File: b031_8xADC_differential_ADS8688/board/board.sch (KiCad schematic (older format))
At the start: 18 parts, among them J1 002_SPI_2x5, J2 007_ADC_2x5, J3 007_ADC_2x5, J4 007_ADC_2x5, J5 007_ADC_2x5, J6 007_ADC_2x5, J7 007_ADC_2x5, J8 007_ADC_2x5, J9 007_ADC_2x5, U1 ADS8688

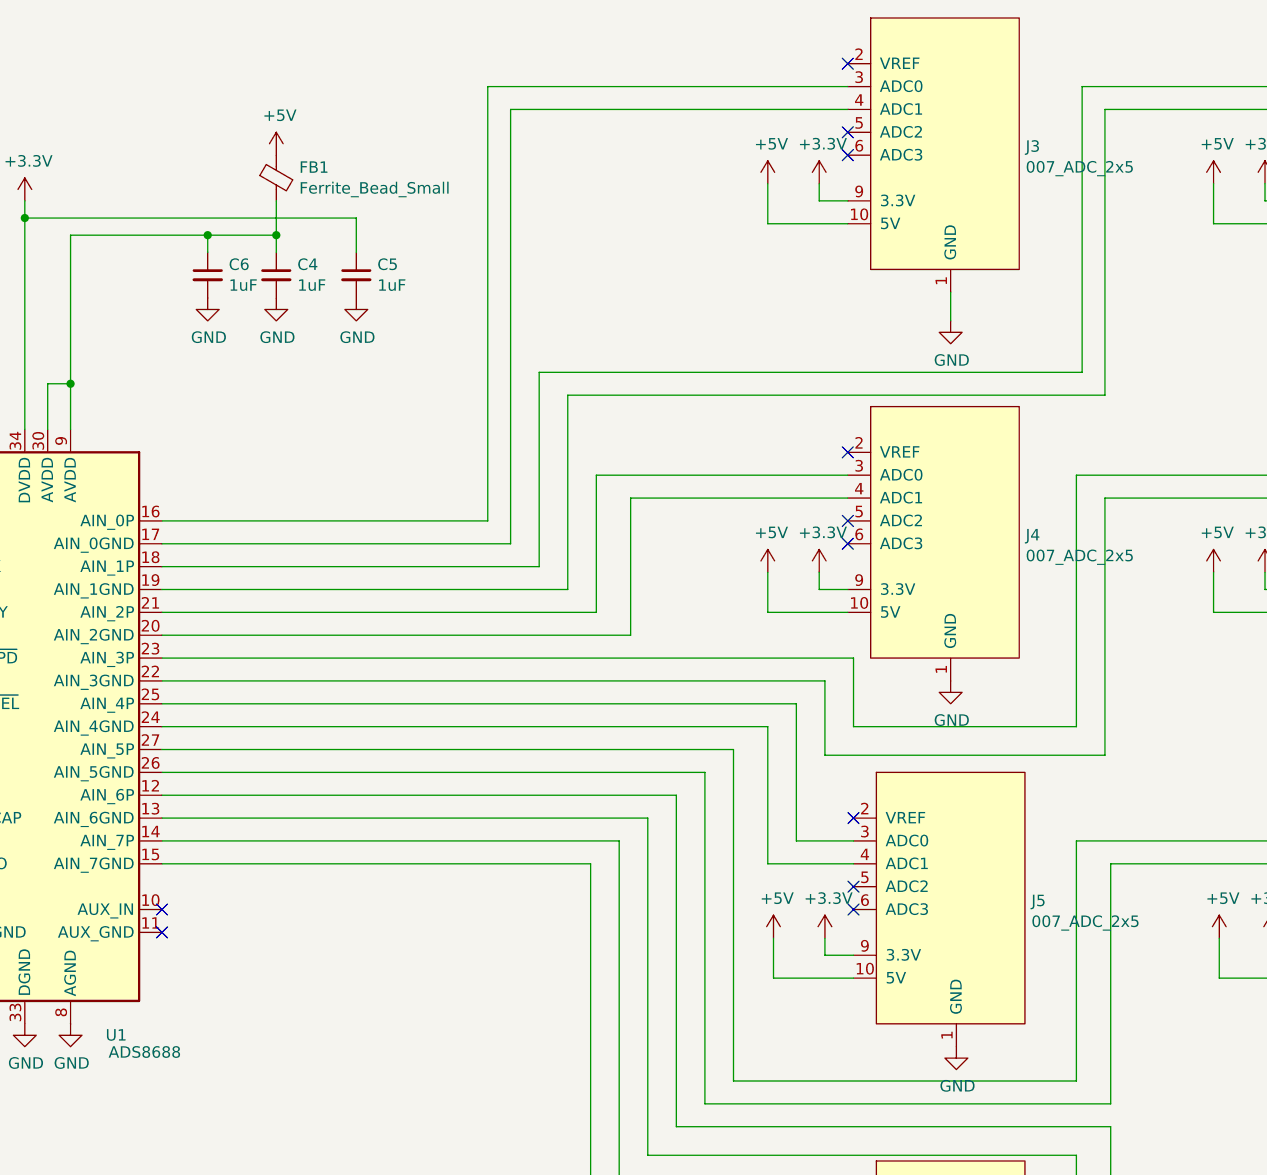
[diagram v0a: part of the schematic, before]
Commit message: added gnd resistors
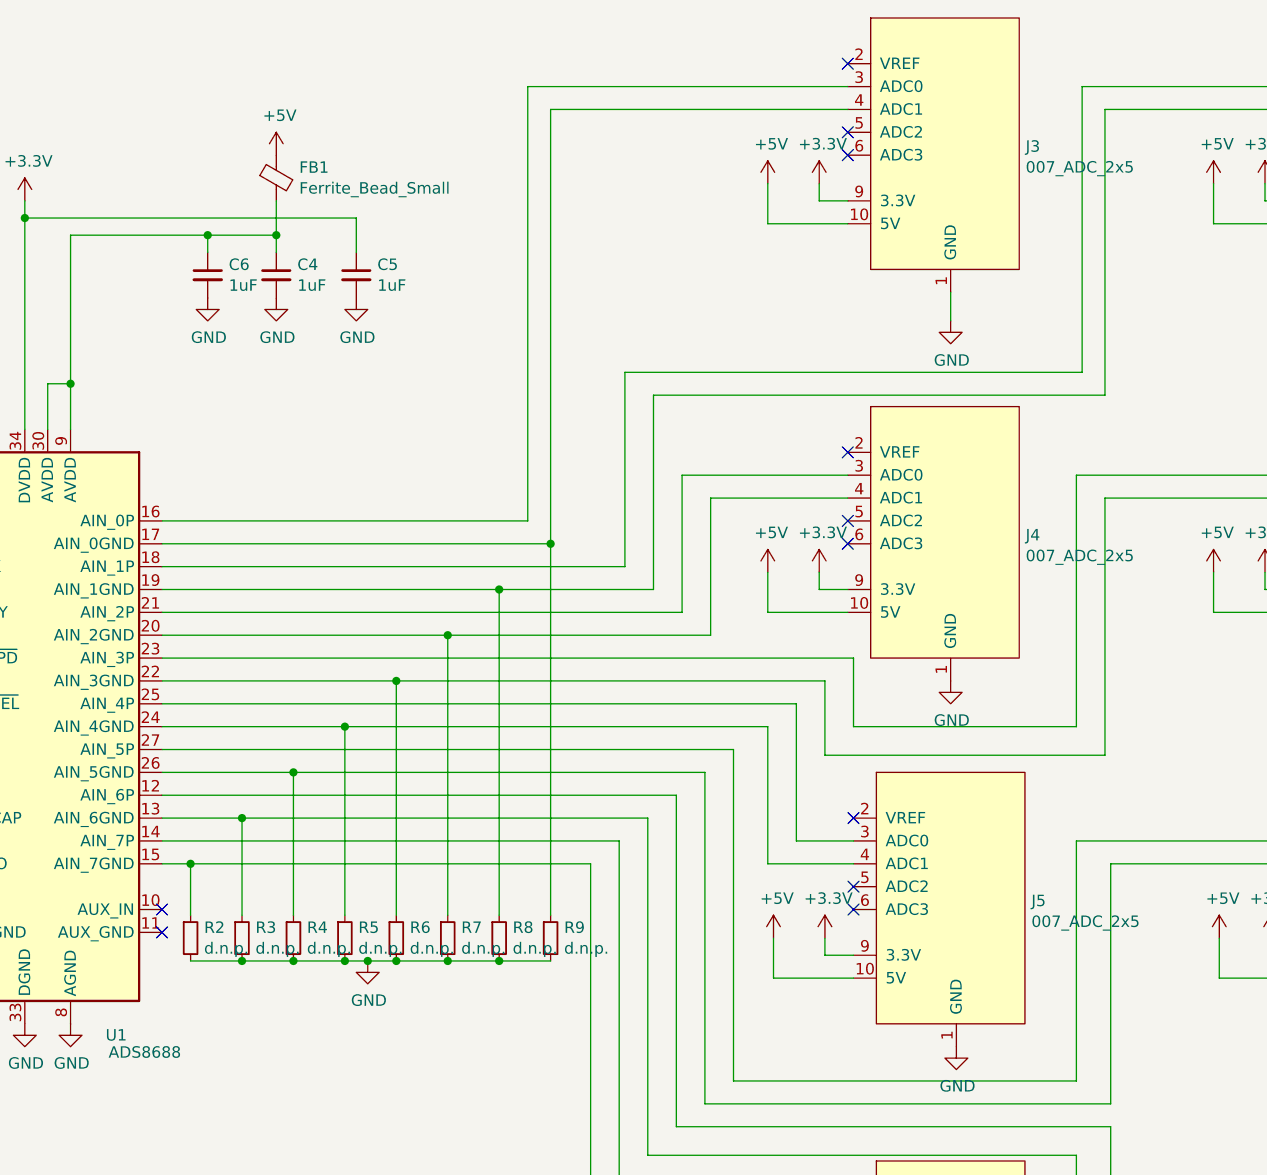
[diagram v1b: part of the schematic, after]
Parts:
- added R2, R3, R4, R5, R6, R7, R8, R9: d.n.p., Resistor_SMD:R_0603_1608Metric, symbol Device:R_Small
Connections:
- net GND: now also R2.2, R3.2, R4.2, R5.2, R6.2, R7.2, R8.2, R9.2
- net at J2.4 (ADC1), U1.13 (AIN_6GND): now also R3.1
- net at J6.4 (ADC1), U1.15 (AIN_7GND): now also R2.1
- net at J3.4 (ADC1), U1.17 (AIN_0GND): now also R9.1
- net at J7.4 (ADC1), U1.19 (AIN_1GND): now also R8.1
- net at J4.4 (ADC1), U1.20 (AIN_2GND): now also R7.1
- net at J8.4 (ADC1), U1.22 (AIN_3GND): now also R6.1
- net at J5.4 (ADC1), U1.24 (AIN_4GND): now also R5.1
- net at J9.4 (ADC1), U1.26 (AIN_5GND): now also R4.1
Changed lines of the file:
@@
 	7275 1275 7400 1275
 Wire Wire Line
-	4400 2675 5825 2675
-Wire Wire Line
-	5825 2675 5825 775
-Wire Wire Line
-	5825 775  7400 775
-Wire Wire Line
-	4400 2775 5925 2775
-Wire Wire Line
-	5925 2775 5925 875
-Wire Wire Line
-	5925 875  7400 875
-Wire Wire Line
-	4400 2875 6050 2875
-Wire Wire Line
-	6050 2875 6050 2025
-Wire Wire Line
-	6050 2025 8425 2025
+	4400 2675 6000 2675
+Wire Wire Line
+	6000 2675 6000 775
+Wire Wire Line
+	6000 775  7400 775
+Wire Wire Line
+	4400 2775 6100 2775
+Wire Wire Line
+	6100 2775 6100 875
+Wire Wire Line
+	6100 875  7400 875
+Wire Wire Line
+	4400 2875 6425 2875
+Wire Wire Line
+	6425 2875 6425 2025
+Wire Wire Line
+	6425 2025 8425 2025
 Wire Wire Line
 	8425 2025 8425 775
@@
 	8425 775  9350 775
 Wire Wire Line
-	4400 2975 6175 2975
-Wire Wire Line
-	6175 2975 6175 2125
-Wire Wire Line
-	6175 2125 8525 2125
+	4400 2975 5875 2975
+Wire Wire Line
+	6550 2975 6550 2125
+Wire Wire Line
+	6550 2125 8525 2125
 Wire Wire Line
 	8525 2125 8525 875
 Wire Wire Line
-	4400 3075 6300 3075
-Wire Wire Line
-	6300 3075 6300 2475
-Wire Wire Line
-	6300 2475 7400 2475
-Wire Wire Line
-	4400 3175 6450 3175
-Wire Wire Line
-	6450 3175 6450 2575
-Wire Wire Line
-	6450 2575 7400 2575
+	4400 3075 6675 3075
+Wire Wire Line
+	6675 3075 6675 2475
+Wire Wire Line
+	6675 2475 7400 2475
+Wire Wire Line
+	4400 3175 5650 3175
+Wire Wire Line
+	6800 3175 6800 2575
+Wire Wire Line
+	6800 2575 7400 2575
 Wire Wire Line
 	4400 3275 7425 3275
@@
 	7300 3700 7300 3375
 Wire Wire Line
-	7300 3375 4400 3375
+	7300 3375 5425 3375
 Wire Wire Line
 	4400 3475 7175 3475
@@
 	7175 3475 7175 4075
 Wire Wire Line
-	4400 3575 7050 3575
+	4400 3575 5200 3575
 Wire Wire Line
 	7050 3575 7050 4175
@@
 	6775 5225 6775 3775
 Wire Wire Line
-	6775 3775 4400 3775
+	6775 3775 4975 3775
 Wire Wire Line
 	8550 5775 8550 5325
@@
 	6525 5450 6525 3975
 Wire Wire Line
-	6525 3975 4400 3975
+	6525 3975 4750 3975
 Wire Wire Line
 	8400 5875 9375 5875
@@
 	6400 5775 7425 5775
 Wire Wire Line
-	4400 4175 6275 4175
+	4400 4175 4525 4175
 Wire Wire Line
 	6275 4175 6275 5875
@@
 Wire Wire Line
 	3100 3075 3400 3075
+$Comp
+L Device:R_Small R2
+U 1 1 609D2BFC
+P 4525 4500
+F 0 "R2" H 4584 4546 50  0000 L CNN
+F 1 "d.n.p." H 4584 4455 50  0000 L CNN
+F 2 "Resistor_SMD:R_0603_1608Metric" H 4525 4500 50  0001 C CNN
+F 3 "~" H 4525 4500 50  0001 C CNN
+	1    4525 4500
+	1    0    0    -1
+$EndComp
+$Comp
+L Device:R_Small R3
+U 1 1 609D3458
+P 4750 4500
+F 0 "R3" H 4809 4546 50  0000 L CNN
+F 1 "d.n.p." H 4809 4455 50  0000 L CNN
+F 2 "Resistor_SMD:R_0603_1608Metric" H 4750 4500 50  0001 C CNN
+F 3 "~" H 4750 4500 50  0001 C CNN
+	1    4750 4500
+	1    0    0    -1
+$EndComp
+$Comp
+L Device:R_Small R4
+U 1 1 609D37DA
+P 4975 4500
+F 0 "R4" H 5034 4546 50  0000 L CNN
+F 1 "d.n.p." H 5034 4455 50  0000 L CNN
+F 2 "Resistor_SMD:R_0603_1608Metric" H 4975 4500 50  0001 C CNN
+F 3 "~" H 4975 4500 50  0001 C CNN
+	1    4975 4500
+	1    0    0    -1
+$EndComp
+$Comp
+L Device:R_Small R5
+U 1 1 609D3BD5
+P 5200 4500
+F 0 "R5" H 5259 4546 50  0000 L CNN
+F 1 "d.n.p." H 5259 4455 50  0000 L CNN
+F 2 "Resistor_SMD:R_0603_1608Metric" H 5200 4500 50  0001 C CNN
+F 3 "~" H 5200 4500 50  0001 C CNN
+	1    5200 4500
+	1    0    0    -1
+$EndComp
+$Comp
+L Device:R_Small R6
+U 1 1 609D6F9D
+P 5425 4500
+F 0 "R6" H 5484 4546 50  0000 L CNN
+F 1 "d.n.p." H 5484 4455 50  0000 L CNN
+F 2 "Resistor_SMD:R_0603_1608Metric" H 5425 4500 50  0001 C CNN
+F 3 "~" H 5425 4500 50  0001 C CNN
+	1    5425 4500
+	1    0    0    -1
+$EndComp
+$Comp
+L Device:R_Small R7
+U 1 1 609D6FA3
+P 5650 4500
+F 0 "R7" H 5709 4546 50  0000 L CNN
+F 1 "d.n.p." H 5709 4455 50  0000 L CNN
+F 2 "Resistor_SMD:R_0603_1608Metric" H 5650 4500 50  0001 C CNN
+F 3 "~" H 5650 4500 50  0001 C CNN
+	1    5650 4500
+	1    0    0    -1
+$EndComp
+$Comp
+L Device:R_Small R8
+U 1 1 609D6FA9
+P 5875 4500
+F 0 "R8" H 5934 4546 50  0000 L CNN
+F 1 "d.n.p." H 5934 4455 50  0000 L CNN
+F 2 "Resistor_SMD:R_0603_1608Metric" H 5875 4500 50  0001 C CNN
+F 3 "~" H 5875 4500 50  0001 C CNN
+	1    5875 4500
+	1    0    0    -1
+$EndComp
+$Comp
+L Device:R_Small R9
+U 1 1 609D6FAF
+P 6100 4500
+F 0 "R9" H 6159 4546 50  0000 L CNN
+F 1 "d.n.p." H 6159 4455 50  0000 L CNN
+F 2 "Resistor_SMD:R_0603_1608Metric" H 6100 4500 50  0001 C CNN
+F 3 "~" H 6100 4500 50  0001 C CNN
+	1    6100 4500
+	1    0    0    -1
+$EndComp
+$Comp
+L power:GND #PWR0142
+U 1 1 609DCCF3
+P 5300 4600
+F 0 "#PWR0142" H 5300 4350 50  0001 C CNN
+F 1 "GND" H 5305 4427 50  0000 C CNN
+F 2 "" H 5300 4600 50  0001 C CNN
+F 3 "" H 5300 4600 50  0001 C CNN
+	1    5300 4600
+	1    0    0    -1
+$EndComp
+Wire Wire Line
+	6100 4600 5875 4600
+Connection ~ 4750 4600
+Wire Wire Line
+	4750 4600 4525 4600
+Connection ~ 4975 4600
+Wire Wire Line
+	4975 4600 4750 4600
+Connection ~ 5200 4600
+Wire Wire Line
+	5200 4600 4975 4600
+Connection ~ 5300 4600
+Wire Wire Line
+	5300 4600 5200 4600
+Connection ~ 5425 4600
+Wire Wire Line
+	5425 4600 5300 4600
+Connection ~ 5650 4600
+Wire Wire Line
+	5650 4600 5425 4600
+Connection ~ 5875 4600
+Wire Wire Line
+	5875 4600 5650 4600
+Wire Wire Line
+	4525 4400 4525 4175
+Connection ~ 4525 4175
+Wire Wire Line
+	4525 4175 6275 4175
+Wire Wire Line
+	4750 4400 4750 3975
+Connection ~ 4750 3975
+Wire Wire Line
+	4750 3975 4400 3975
+Wire Wire Line
+	4975 4400 4975 3775
+Connection ~ 4975 3775
+Wire Wire Line
+	4975 3775 4400 3775
+Wire Wire Line
+	5200 4400 5200 3575
+Connection ~ 5200 3575
+Wire Wire Line
+	5200 3575 7050 3575
+Wire Wire Line
+	5425 4400 5425 3375
+Connection ~ 5425 3375
+Wire Wire Line
+	5425 3375 4400 3375
+Wire Wire Line
+	5650 4400 5650 3175
+Connection ~ 5650 3175
+Wire Wire Line
+	5650 3175 6800 3175
+Wire Wire Line
+	5875 4400 5875 2975
+Connection ~ 5875 2975
+Wire Wire Line
+	5875 2975 6550 2975
+Wire Wire Line
+	6100 4400 6100 2775
+Connection ~ 6100 2775
 $EndSCHEMATC
